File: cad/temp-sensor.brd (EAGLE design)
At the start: 69.5 x 40.6 mm, 62 parts, among them J2 455-1750-1-ND, Q1 300S14-U, Q2 320S14-U, Q3 320S14-U, U1 SE555D, U2 SE555D, U4 MCP6001UT-I/OT, U5 MCP6001UT-I/OT, U6 MCP6001UT-I/OT, U7 MCP6001UT-I/OT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

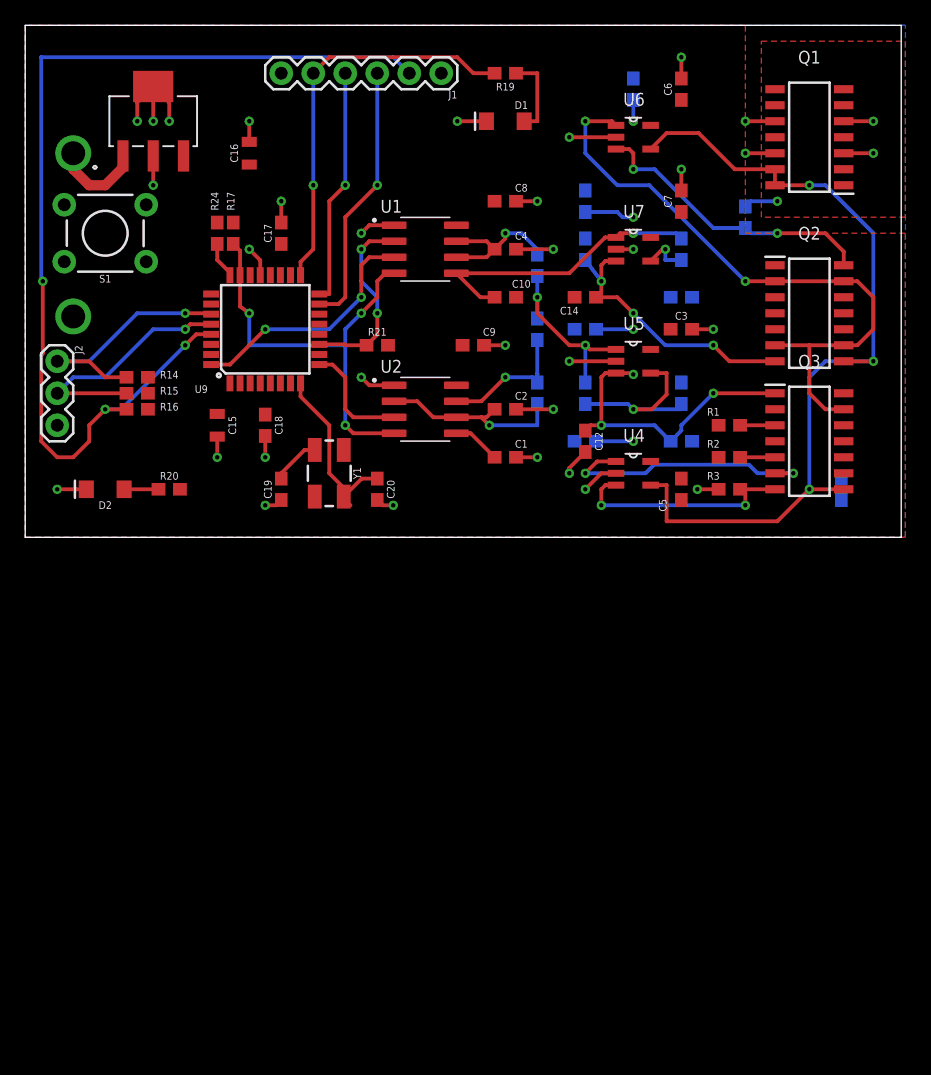
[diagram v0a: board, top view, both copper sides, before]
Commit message: Clean up silk and add test points
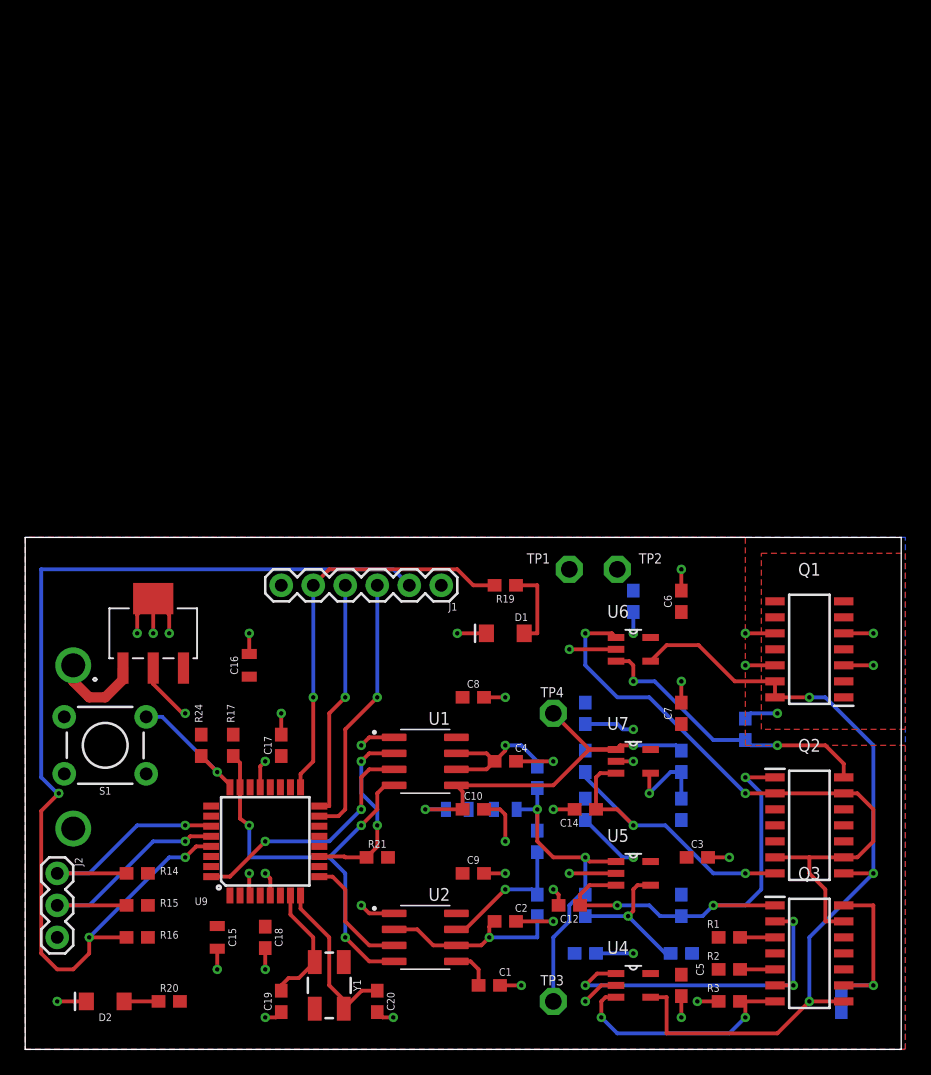
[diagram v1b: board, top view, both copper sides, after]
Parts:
- added C11, C13: 10uF, SparkFun-Capacitors:0805
- added TP1, TP2, TP3, TP4: TPPAD1-13, testpad:P1-13
- moved R5 44.5 mm to (52.1, 7.62), turned to 0 degrees
- moved C1 41.9 mm to (36.8, 5.08)
- moved C3 41.9 mm to (53.3, 15.2)
- moved C9 41.9 mm to (35.6, 14.0)
- moved R16 41.9 mm to (8.89, 8.89)
- moved U2 41.9 mm to (31.8, 8.89)
- moved C10 40.7 mm to (35.6, 19.1)
- moved R24 40.7 mm to (14.0, 24.1)
- moved R8 40.6 mm to (57.1, 25.4)
- moved BT1 40.6 mm to (3.81, 30.5)
- moved C14 40.6 mm to (44.5, 19.1)
- moved C15 40.6 mm to (15.2, 8.89)
- moved C16 40.6 mm to (17.8, 30.5)
- moved C17 40.6 mm to (20.3, 24.1)
- moved C18 40.6 mm to (19.1, 8.89)
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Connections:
- net +5V: now also TP1.TP
- net GND: now also C11.2, C13.2, TP2.TP
- net VBG_REF: now also C11.1, TP3.TP
- net VPTAT_REF: now also C13.1, TP4.TP
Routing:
- net START_C: track 0.00 -> 13.8 mm, vias 0 -> 1
- net GND: track 75.1 -> 87.6 mm, vias 33 -> 38
- net I_BG: track 24.2 -> 36.3 mm
- net VBG_REF: track 15.9 -> 27.2 mm
- net VPTAT_REF: track 23.6 -> 32.2 mm, vias 1 -> 2
- net PBTN: track 2.90 -> 10.9 mm, vias 0 -> 1
- net XTAL1: track 3.85 -> 9.93 mm
- net CTAT_BASE: track 21.4 -> 27.3 mm, vias 2 -> 3
- net I_PTAT: track 22.4 -> 26.4 mm, vias 3 -> 2
- net PTAT_REF_FB: track 3.68 -> 6.99 mm
- net BG_REF_FB: track 14.3 -> 11.8 mm
- net MCU_RST: track 80.9 -> 83.2 mm
- net TEMP_VBE: track 68.5 -> 66.3 mm
- net +5V: track 11.6 -> 13.7 mm
- net CTAT_IN+: track 18.0 -> 19.1 mm
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
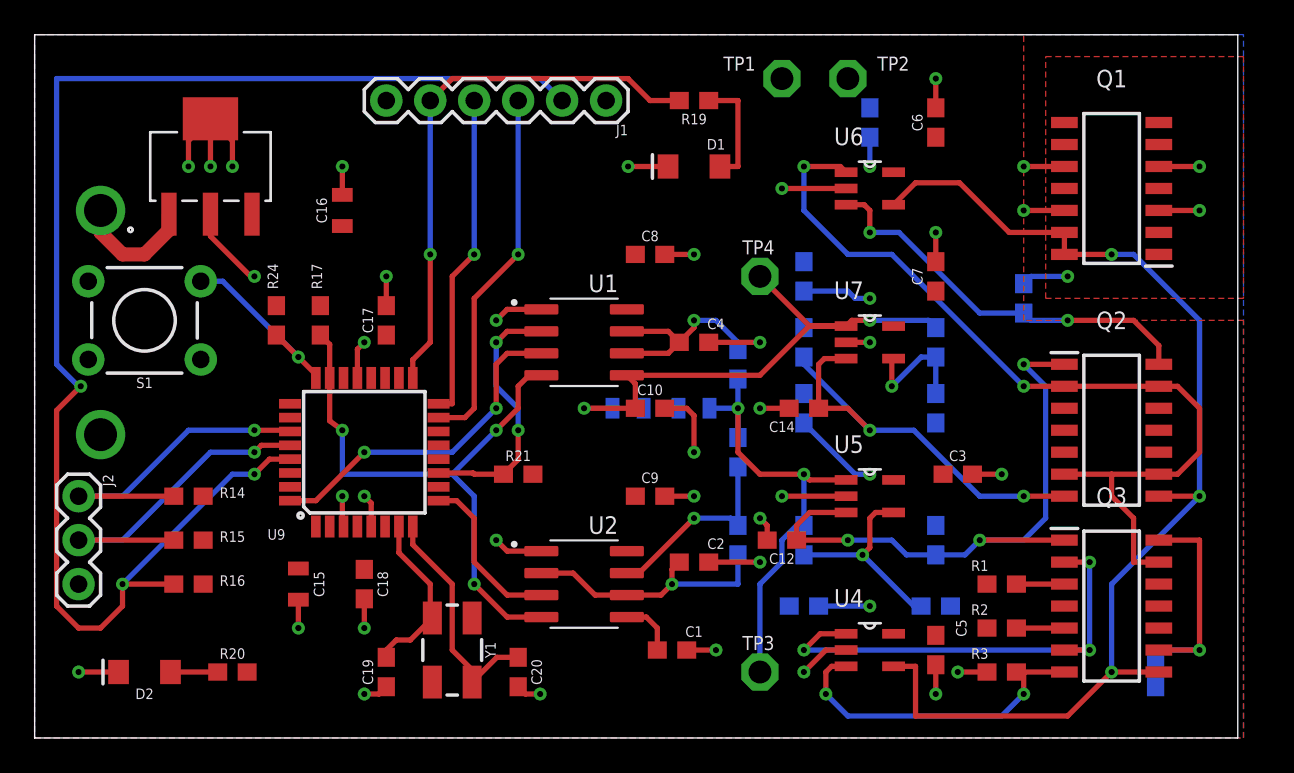
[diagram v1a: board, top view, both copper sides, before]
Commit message: Add 4 pin header for OLED
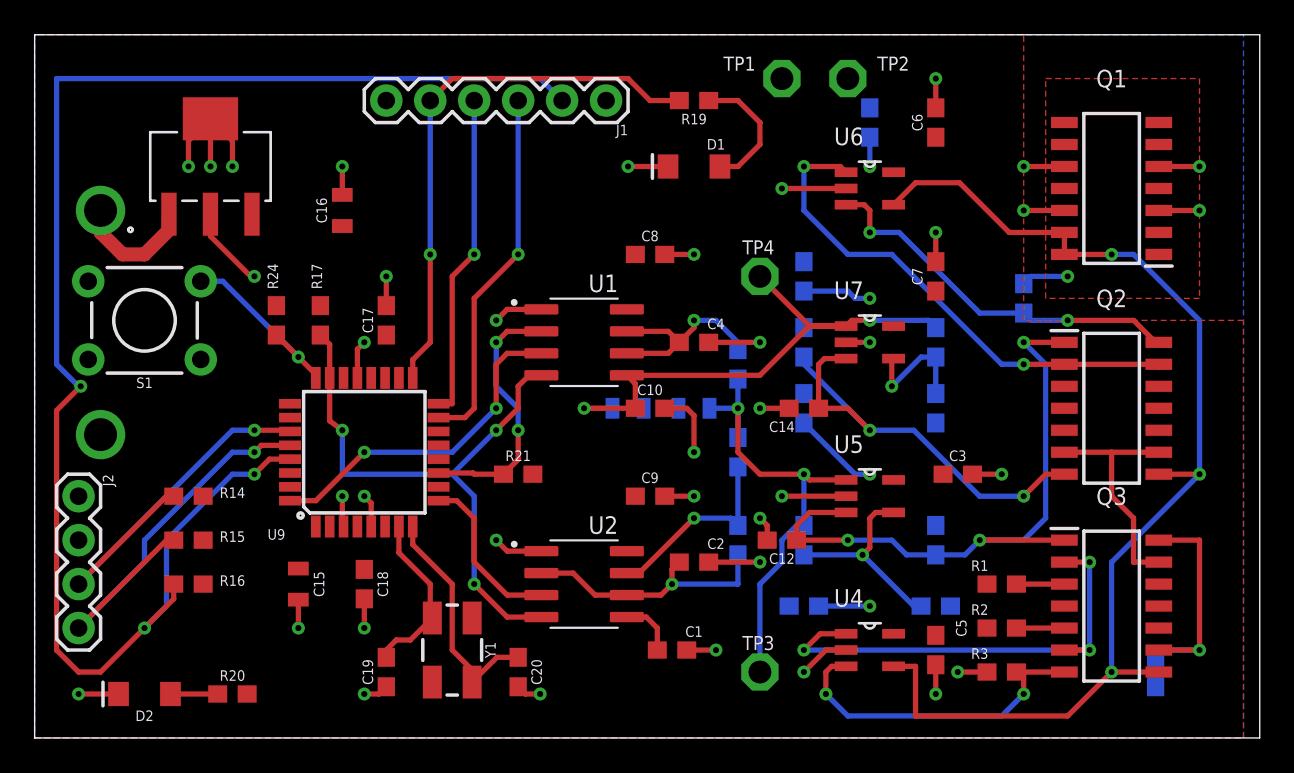
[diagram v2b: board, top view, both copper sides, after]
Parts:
- J2: value 455-1750-1-ND -> (none); device SparkFun-Connectors:1X03 -> SparkFun-Connectors:1X04
- moved D2 1.27 mm to (6.35, 2.54)
- moved R20 1.27 mm to (11.4, 2.54)
- moved Q2 1.27 mm to (62.2, 19.1)
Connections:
- net +5V: now also J2.1
- net GND: now also J2.2; no longer J2.3
- net SCL: now also J2.4; no longer J2.2
- net SDA: now also J2.3; no longer J2.1
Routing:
- net PTAT_BASE: track 50.6 -> 43.3 mm
- net MCU_RST: track 83.2 -> 88.6 mm
- net SCL: track 20.0 -> 24.9 mm
- net SDA: track 19.3 -> 23.5 mm
- net I_BG: track 36.3 -> 37.6 mm
- net PTAT_IN+: track 23.3 -> 22.1 mm
- net N$2: track 6.54 -> 7.59 mm
- net I_PTAT: track 26.4 -> 26.9 mm
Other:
- board size 69.5 x 40.6 mm -> 70.8 x 40.6 mm

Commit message: Finishing touches on silk
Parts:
- added R22: 10k, SparkFun-Resistors:0603
- moved R19 1.80 mm to (36.8, 38.1)
- moved D1 1.27 mm to (36.8, 33.0)
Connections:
- net GND: now also R22.1
- net SS: now also R22.2
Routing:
- net SS: track 0.00 -> 3.23 mm, vias 0 -> 1
- net SCK: track 31.9 -> 30.1 mm
- net N$2: track 7.59 -> 8.86 mm
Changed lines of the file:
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@@
 <layer number="20" name="Dimension" color="24" fill="1" visible="yes" active="yes"/>
 <layer number="21" name="tPlace" color="7" fill="1" visible="yes" active="yes"/>
-<layer number="22" name="bPlace" color="7" fill="1" visible="no" active="yes"/>
+<layer number="22" name="bPlace" color="7" fill="1" visible="yes" active="yes"/>
 <layer number="23" name="tOrigins" color="15" fill="1" visible="yes" active="yes"/>
-<layer number="24" name="bOrigins" color="15" fill="1" visible="no" active="yes"/>
+<layer number="24" name="bOrigins" color="15" fill="1" visible="yes" active="yes"/>
 <layer number="25" name="tNames" color="7" fill="1" visible="yes" active="yes"/>
-<layer number="26" name="bNames" color="7" fill="1" visible="no" active="yes"/>
+<layer number="26" name="bNames" color="7" fill="1" visible="yes" active="yes"/>
 <layer number="27" name="tValues" color="7" fill="1" visible="yes" active="yes"/>
-<layer number="28" name="bValues" color="7" fill="1" visible="no" active="yes"/>
+<layer number="28" name="bValues" color="7" fill="1" visible="yes" active="yes"/>
 <layer number="29" name="tStop" color="7" fill="3" visible="no" active="yes"/>
 <layer number="30" name="bStop" color="7" fill="6" visible="no" active="yes"/>
@@
 <layer number="38" name="bTest" color="7" fill="1" visible="no" active="yes"/>
 <layer number="39" name="tKeepout" color="4" fill="11" visible="yes" active="yes"/>
-<layer number="40" name="bKeepout" color="1" fill="11" visible="no" active="yes"/>
+<layer number="40" name="bKeepout" color="1" fill="11" visible="yes" active="yes"/>
 <layer number="41" name="tRestrict" color="4" fill="10" visible="no" active="yes"/>
 <layer number="42" name="bRestrict" color="1" fill="10" visible="no" active="yes"/>
@@
 <layer number="50" name="dxf" color="7" fill="1" visible="no" active="no"/>
 <layer number="51" name="tDocu" color="7" fill="1" visible="yes" active="yes"/>
-<layer number="52" name="bDocu" color="7" fill="1" visible="no" active="yes"/>
+<layer number="52" name="bDocu" color="7" fill="1" visible="yes" active="yes"/>
 <layer number="53" name="tGND_GNDA" color="7" fill="9" visible="no" active="no"/>
 <layer number="54" name="bGND_GNDA" color="1" fill="9" visible="no" active="no"/>
@@
 <attribute name="VALUE" x="35.56" y="13.208" size="0.6096" layer="27" font="vector" ratio="20" align="top-center"/>
 </element>
-<element name="D1" library="SparkFun-LED" library_urn="urn:adsk.eagle:library:529" package="LED-1206" package3d_urn="urn:adsk.eagle:package:39352/2" value="SCK" x="38.1" y="33.02" smashed="yes" rot="R180">
-<attribute name="NAME" x="39.37" y="34.6075" size="0.6096" layer="25" font="vector" ratio="20" rot="R180" align="bottom-center"/>
-<attribute name="PROD_ID" value="DIO-00862" x="-34.29" y="132.08" size="1.778" layer="27" rot="R180" display="off"/>
-<attribute name="VALUE" x="36.83" y="34.6075" size="0.6096" layer="27" font="vector" ratio="20" align="top-center"/>
+<element name="D1" library="SparkFun-LED" library_urn="urn:adsk.eagle:library:529" package="LED-1206" package3d_urn="urn:adsk.eagle:package:39352/2" value="SCK" x="36.83" y="33.02" smashed="yes" rot="R180">
+<attribute name="NAME" x="38.1" y="34.6075" size="0.6096" layer="25" font="vector" ratio="20" rot="R180" align="bottom-center"/>
+<attribute name="PROD_ID" value="DIO-00862" x="-35.56" y="132.08" size="1.778" layer="27" rot="R180" display="off"/>
+<attribute name="VALUE" x="35.56" y="34.6075" size="0.6096" layer="27" font="vector" ratio="20" align="top-center"/>
 </element>
 <element name="D2" library="SparkFun-LED" library_urn="urn:adsk.eagle:library:529" package="LED-1206" package3d_urn="urn:adsk.eagle:package:39352/2" value="POWER" x="6.35" y="2.54" smashed="yes" rot="R180">
@@
 <attribute name="VALUE" x="65.532" y="3.81" size="0.6096" layer="28" font="vector" ratio="20" rot="MR270" align="top-center"/>
 </element>
-<element name="R19" library="SparkFun-Resistors" library_urn="urn:adsk.eagle:library:532" package="0603" package3d_urn="urn:adsk.eagle:package:41389018/1" value="330" x="38.1" y="36.83" smashed="yes" rot="R180">
-<attribute name="NAME" x="38.1" y="36.068" size="0.6096" layer="25" font="vector" ratio="20" rot="R180" align="bottom-center"/>
-<attribute name="PROD_ID" value="RES-00818" x="-41.91" y="149.86" size="1.778" layer="27" rot="R180" display="off"/>
-<attribute name="VALUE" x="38.1" y="37.592" size="0.6096" layer="27" font="vector" ratio="20" rot="R180" align="top-center"/>
+<element name="R19" library="SparkFun-Resistors" library_urn="urn:adsk.eagle:library:532" package="0603" package3d_urn="urn:adsk.eagle:package:41389018/1" value="330" x="36.83" y="38.1" smashed="yes" rot="R180">
+<attribute name="NAME" x="36.83" y="37.338" size="0.6096" layer="25" font="vector" ratio="20" rot="R180" align="bottom-center"/>
+<attribute name="PROD_ID" value="RES-00818" x="-43.18" y="151.13" size="1.778" layer="27" rot="R180" display="off"/>
+<attribute name="VALUE" x="36.83" y="38.862" size="0.6096" layer="27" font="vector" ratio="20" rot="R180" align="top-center"/>
 </element>
 <element name="R1" library="SparkFun-Resistors" library_urn="urn:adsk.eagle:library:532" package="0603" package3d_urn="urn:adsk.eagle:package:41389018/1" value="1k" x="55.88" y="8.89" smashed="yes" rot="R180">
@@
 <attribute name="PROD_ID" value="CONN-09696" x="2.54" y="13.97" size="1.778" layer="27" rot="R270" display="off"/>
 <attribute name="VALUE" x="0.508" y="15.24" size="0.6096" layer="27" font="vector" ratio="20" rot="R270"/>
+</element>
+<element name="R22" library="SparkFun-Resistors" library_urn="urn:adsk.eagle:library:532" package="0603" package3d_urn="urn:adsk.eagle:package:41389018/1" value="10k" x="20.32" y="19.05" smashed="yes" rot="MR180">
+<attribute name="NAME" x="20.32" y="18.288" size="0.6096" layer="26" font="vector" ratio="20" rot="MR180" align="bottom-center"/>
+<attribute name="PROD_ID" value="RES-00824" x="20.32" y="19.05" size="1.778" layer="28" rot="MR180" display="off"/>
+<attribute name="VALUE" x="20.32" y="19.812" size="0.6096" layer="28" font="vector" ratio="20" rot="MR180" align="top-center"/>
 </element>
 </elements>
@@
 <via x="52.07" y="38.1" extent="1-16" drill="0.35"/>
 <via x="52.07" y="29.21" extent="1-16" drill="0.35"/>
-<wire x1="36.6" y1="33.02" x2="34.29" y2="33.02" width="0.3048" layer="1"/>
-<via x="34.29" y="33.02" extent="1-16" drill="0.35"/>
+<wire x1="35.33" y1="33.02" x2="33.02" y2="33.02" width="0.3048" layer="1"/>
+<via x="33.02" y="33.02" extent="1-16" drill="0.35"/>
 <wire x1="52.07" y1="27.52" x2="52.07" y2="29.21" width="0.3048" layer="1"/>
 <wire x1="20.32" y1="24.98" x2="20.32" y2="26.67" width="0.3048" layer="1"/>
@@
 <contactref element="TP2" pad="TP"/>
 <contactref element="J2" pad="2"/>
+<contactref element="R22" pad="1"/>
 </signal>
 <signal name="+5V">
@@
 <wire x1="22.86" y1="36.83" x2="22.86" y2="27.94" width="0.3048" layer="16"/>
 <via x="22.86" y="27.94" extent="1-16" drill="0.35"/>
-<wire x1="37.25" y1="36.83" x2="35.56" y2="36.83" width="0.3048" layer="1"/>
-<wire x1="35.56" y1="36.83" x2="34.29" y2="38.1" width="0.3048" layer="1"/>
-<wire x1="34.29" y1="38.1" x2="24.13" y2="38.1" width="0.3048" layer="1"/>
+<wire x1="35.98" y1="38.1" x2="24.13" y2="38.1" width="0.3048" layer="1"/>
 <wire x1="21.85" y1="20.8026" x2="21.85" y2="21.85" width="0.3048" layer="1"/>
 <wire x1="21.85" y1="21.85" x2="22.86" y2="22.86" width="0.3048" layer="1"/>
@@
 <signal name="SS">
 <contactref element="U9" pad="14"/>
+<contactref element="R22" pad="2"/>
+<wire x1="23.3426" y1="17.71" x2="21.66" y2="17.71" width="0.3048" layer="1"/>
+<wire x1="21.66" y1="17.71" x2="21.59" y2="17.78" width="0.3048" layer="1"/>
+<via x="21.59" y="17.78" extent="1-16" drill="0.35"/>
+<wire x1="21.59" y1="17.78" x2="21.17" y2="18.2" width="0.3048" layer="16"/>
+<wire x1="21.17" y1="18.2" x2="21.17" y2="19.05" width="0.3048" layer="16"/>
 </signal>
 <signal name="555_RST_N">
@@
 <contactref element="R19" pad="1"/>
 <contactref element="D1" pad="A"/>
-<wire x1="38.95" y1="36.83" x2="40.64" y2="36.83" width="0.3048" layer="1"/>
-<wire x1="40.64" y1="36.83" x2="41.91" y2="35.56" width="0.3048" layer="1"/>
-<wire x1="41.91" y1="34.29" x2="41.91" y2="35.56" width="0.3048" layer="1"/>
-<wire x1="41.91" y1="34.29" x2="40.64" y2="33.02" width="0.3048" layer="1"/>
-<wire x1="40.64" y1="33.02" x2="39.6" y2="33.02" width="0.3048" layer="1"/>
+<wire x1="38.33" y1="33.02" x2="39.37" y2="33.02" width="0.3048" layer="1"/>
+<wire x1="39.37" y1="33.02" x2="40.64" y2="34.29" width="0.3048" layer="1"/>
+<wire x1="40.64" y1="34.29" x2="40.64" y2="36.83" width="0.3048" layer="1"/>
+<wire x1="40.64" y1="36.83" x2="39.37" y2="38.1" width="0.3048" layer="1"/>
+<wire x1="39.37" y1="38.1" x2="37.68" y2="38.1" width="0.3048" layer="1"/>
 </signal>
 <signal name="N$3">

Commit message: Removed +5V power plane
Removed +5V power plane. Instead, +5V was routed with 12 mil traces
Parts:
- moved C2 2.54 mm to (38.1, 7.62)
- moved R8 1.80 mm to (55.9, 26.7), flipped to the top
- moved J2 1.27 mm to (3.81, 14.0)
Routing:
- net +5V: track 13.7 -> 257.2 mm
- net 3_NPN_DIODE: track 2.71 -> 30.1 mm, vias 1 -> 0
- net PTAT_BASE: track 43.3 -> 50.6 mm
- net I_PTAT: track 26.9 -> 24.1 mm
- net I_BG: track 37.6 -> 35.0 mm
- net VBG_REF: track 27.2 -> 25.7 mm
- net SDA: track 23.5 -> 22.2 mm
- net SCL: track 24.9 -> 23.6 mm
- net FREQ_DIS: track 11.3 -> 12.0 mm
- net PTAT_IN+: track 22.1 -> 21.4 mm, vias 2 -> 0
- net PTAT_REF_FB: track 6.99 -> 6.47 mm
- removed copper zone on layer 1, net +5V
- removed copper zone on layer 1, net 3_NPN_DIODE

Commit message: Presentation comments
Removed V_BG buffer. Now feeding I_BG current source to input capacitor of monostable timer. Rerouted with 6 mil traces.
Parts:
- removed C11: 10uF, SparkFun-Capacitors:0805
- removed C12, C3: 10nF, SparkFun-Capacitors:0603
- removed C24: 1.0uF, SparkFun-Capacitors:0603
- removed R12: 10k, SparkFun-Resistors:0603
- removed R4: 100k, SparkFun-Resistors:0603
- removed R5: 200k, SparkFun-Resistors:0603
- removed R7: 5.1k, SparkFun-Resistors:0603
- removed TP3: TPPAD1-13, testpad:P1-13
- removed U5: MCP6001UT-I/OT, MCP6001UT-I_OT:SOT95P270X145-5N
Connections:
- removed net BG_REF_FB: R4.1, R5.2, U5.4
- removed net PULSE_THRES: C4.1, R12.1, U1.6, U1.7
- removed net VBG_REF: C11.1, R10.2, R12.2, R4.2, TP3.TP, U5.1
- net +5V: now also R10.2; no longer C24.1, C3.1, U5.5
- net GND: no longer C11.2, C12.2, C24.2, C3.2, R5.1, R7.1, U5.2
- net I_BG: now also C4.1, U1.6, U1.7; no longer C12.1, R7.2, U5.3
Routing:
- net VBG_REF: track 25.7 -> 0.00 mm, vias 2 -> 0
- net BG_REF_FB: track 11.8 -> 0.00 mm, vias 1 -> 0
- net PULSE_THRES: track 11.7 -> 0.00 mm, vias 1 -> 0
- net +5V: track 257.2 -> 246.0 mm, vias 4 -> 3
- net GND: track 87.4 -> 80.6 mm, vias 38 -> 35
- net I_BG: track 35.0 -> 31.3 mm
